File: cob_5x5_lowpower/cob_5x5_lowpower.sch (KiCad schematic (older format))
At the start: 19 parts, among them J1 Conn_01x03, J2 Conn_01x03, Q1 Q_PMOS_GSD, Q2 Q_PMOS_GSD, Q3 Q_PMOS_GSD, U1 WS2811

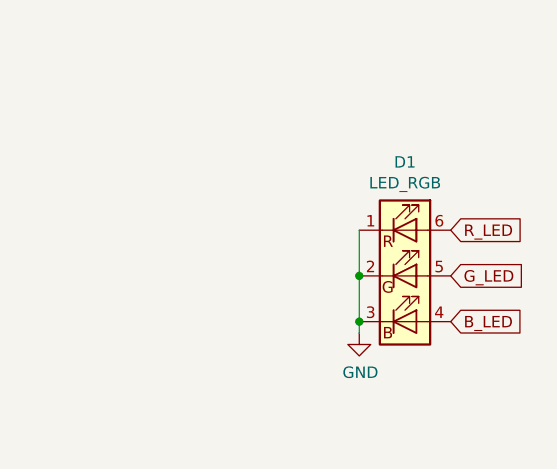
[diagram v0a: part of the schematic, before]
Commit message: Lowpower one-off revision 1.0.
Updated previous attempt (unfabricated) with lessons from from
high-power board.
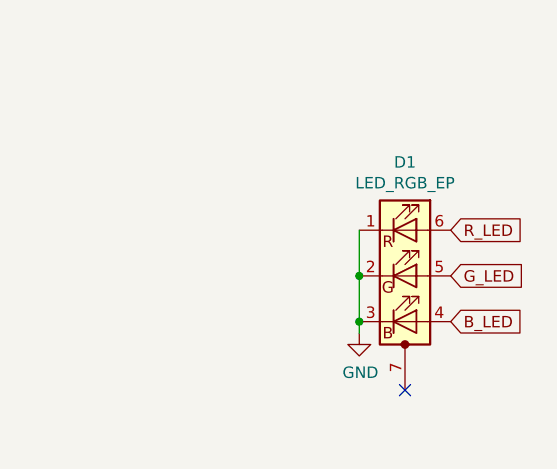
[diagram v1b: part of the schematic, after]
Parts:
- removed D1: LED_RGB, LED_SMD:LED_RGB_Getian_GT-P6PRGB4303, symbol Device:LED_RGB
- added D1: LED_RGB_EP, homebrew:LED_RGB_EPISTAR_6PIN_RGB, symbol Device:LED_RGB_EP
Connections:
- net B_LED: now also D1.4 (BA)
- net GND: now also D1.1 (RK), D1.2 (GK), D1.3 (BK)
- net G_LED: now also D1.5 (GA)
- net R_LED: now also D1.6 (RA)
- no-connect marks 1 -> 2
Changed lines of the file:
@@
-	1    0    0    -1
-$EndComp
-$Comp
-L Device:LED_RGB D1
-U 1 1 5DC2FA10
-P 7000 3500
-F 0 "D1" H 7000 3997 50  0000 C CNN
-F 1 "LED_RGB" H 7000 3906 50  0000 C CNN
-F 2 "LED_SMD:LED_RGB_Getian_GT-P6PRGB4303" H 7000 3450 50  0001 C CNN
-F 3 "~" H 7000 3450 50  0001 C CNN
-	1    7000 3500
 	1    0    0    -1
 $EndComp
@@
 	1    0    0    -1
 $EndComp
-Wire Wire Line
-	6800 3300 6800 3500
-Wire Wire Line
-	6800 3500 6800 3700
-Connection ~ 6800 3500
-Wire Wire Line
-	6800 3750 6800 3700
-Connection ~ 6800 3700
 $Comp
 L Device:Q_PMOS_GSD Q1
@@
 	1    0    0    -1
 $EndComp
+$Comp
+L Device:LED_RGB_EP D1
+U 1 1 5DD5AA88
+P 7000 3500
+F 0 "D1" H 7000 3997 50  0000 C CNN
+F 1 "LED_RGB_EP" H 7000 3906 50  0000 C CNN
+F 2 "homebrew:LED_RGB_EPISTAR_6PIN_RGB" H 7000 3450 50  0001 C CNN
+F 3 "~" H 7000 3450 50  0001 C CNN
+	1    7000 3500
+	1    0    0    -1
+$EndComp
+Wire Wire Line
+	6800 3700 6800 3750
+Wire Wire Line
+	6800 3700 6800 3500
+Connection ~ 6800 3700
+Wire Wire Line
+	6800 3500 6800 3300
+Connection ~ 6800 3500
+NoConn ~ 7000 4000
 $EndSCHEMATC
